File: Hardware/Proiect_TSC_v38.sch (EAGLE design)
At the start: 103 parts, among them IC1 XC6220A331MR-G, IC2 BD5229G-TR, J1 SAMACSYS_PARTS_USB4110-GF-A, J2 112A-TAAR-R03_ATTEND, J3 FH34SRJ-24S-0.5SH_99_, J4 QWIIC_RIGHT_ANGLE, Q1 20V/4.2A/52mΩ/1.4W, Q2 SI1308EDL-T1-GE3, Q3 20V/4.2A/52mΩ/1.4W, U1 ESP32-C6-WROOM-1-N8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

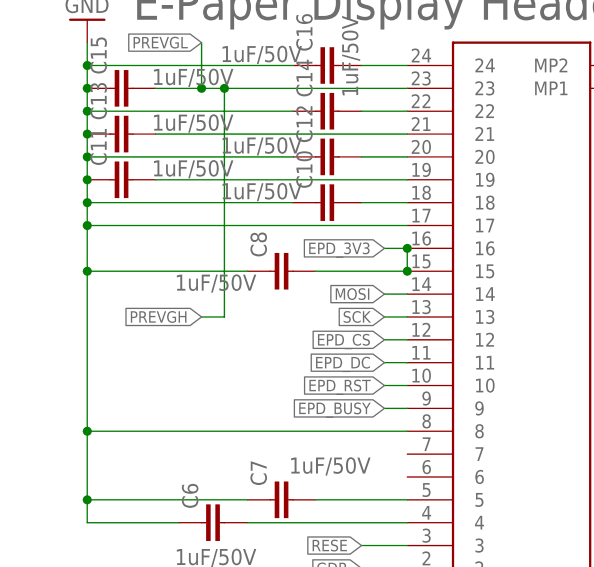
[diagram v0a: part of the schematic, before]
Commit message: update capacitor value
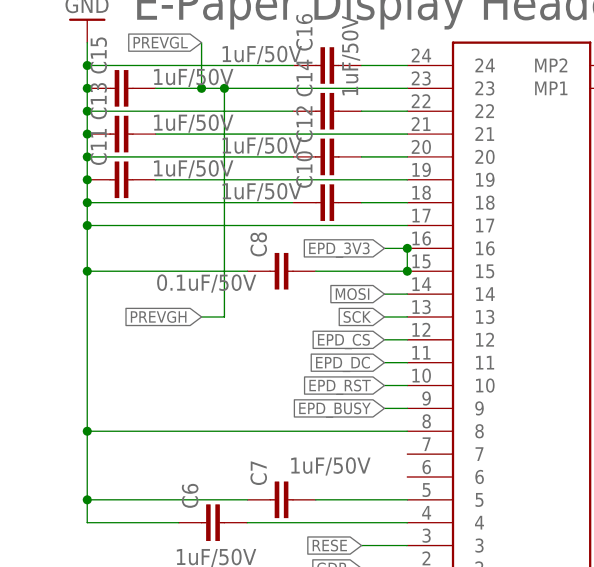
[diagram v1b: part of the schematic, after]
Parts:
- C8: value 1uF/50V -> 0.1uF/50V
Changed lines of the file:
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@@
 <part name="C6" library="DeskAssistant v19 v1" library_urn="urn:adsk.wipprod:fs.file:vf.7Qd4d4l7T_yn8RiDKkSmKA" deviceset="EAGLE-LTSPICE_C" device="C0402" value="1uF/50V"/>
 <part name="C7" library="DeskAssistant v19 v1" library_urn="urn:adsk.wipprod:fs.file:vf.7Qd4d4l7T_yn8RiDKkSmKA" deviceset="EAGLE-LTSPICE_C" device="C0402" value="1uF/50V"/>
-<part name="C8" library="DeskAssistant v19 v1" library_urn="urn:adsk.wipprod:fs.file:vf.7Qd4d4l7T_yn8RiDKkSmKA" deviceset="EAGLE-LTSPICE_C" device="C0402" value="1uF/50V"/>
+<part name="C8" library="DeskAssistant v19 v1" library_urn="urn:adsk.wipprod:fs.file:vf.7Qd4d4l7T_yn8RiDKkSmKA" deviceset="EAGLE-LTSPICE_C" device="C0402" value="0.1uF/50V"/>
 <part name="C10" library="DeskAssistant v19 v1" library_urn="urn:adsk.wipprod:fs.file:vf.7Qd4d4l7T_yn8RiDKkSmKA" deviceset="EAGLE-LTSPICE_C" device="C0402" value="1uF/50V"/>
 <part name="C11" library="DeskAssistant v19 v1" library_urn="urn:adsk.wipprod:fs.file:vf.7Qd4d4l7T_yn8RiDKkSmKA" deviceset="EAGLE-LTSPICE_C" device="C0402" value="1uF/50V"/>

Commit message: Solved wrong routes, added ground plane, fixed silkscreen
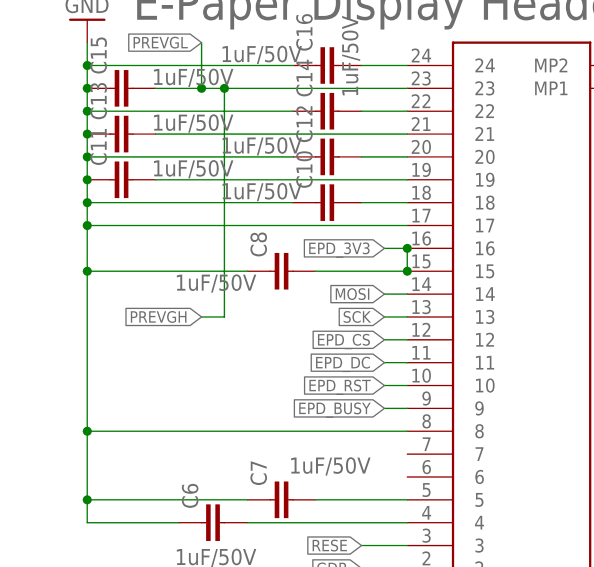
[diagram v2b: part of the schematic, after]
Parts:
- C8: value 0.1uF/50V -> 1uF/50V
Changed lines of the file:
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@@
 <part name="C6" library="DeskAssistant v19 v1" library_urn="urn:adsk.wipprod:fs.file:vf.7Qd4d4l7T_yn8RiDKkSmKA" deviceset="EAGLE-LTSPICE_C" device="C0402" value="1uF/50V"/>
 <part name="C7" library="DeskAssistant v19 v1" library_urn="urn:adsk.wipprod:fs.file:vf.7Qd4d4l7T_yn8RiDKkSmKA" deviceset="EAGLE-LTSPICE_C" device="C0402" value="1uF/50V"/>
-<part name="C8" library="DeskAssistant v19 v1" library_urn="urn:adsk.wipprod:fs.file:vf.7Qd4d4l7T_yn8RiDKkSmKA" deviceset="EAGLE-LTSPICE_C" device="C0402" value="0.1uF/50V"/>
+<part name="C8" library="DeskAssistant v19 v1" library_urn="urn:adsk.wipprod:fs.file:vf.7Qd4d4l7T_yn8RiDKkSmKA" deviceset="EAGLE-LTSPICE_C" device="C0402" value="1uF/50V"/>
 <part name="C10" library="DeskAssistant v19 v1" library_urn="urn:adsk.wipprod:fs.file:vf.7Qd4d4l7T_yn8RiDKkSmKA" deviceset="EAGLE-LTSPICE_C" device="C0402" value="1uF/50V"/>
 <part name="C11" library="DeskAssistant v19 v1" library_urn="urn:adsk.wipprod:fs.file:vf.7Qd4d4l7T_yn8RiDKkSmKA" deviceset="EAGLE-LTSPICE_C" device="C0402" value="1uF/50V"/>
